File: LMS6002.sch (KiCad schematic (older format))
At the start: 52 parts, among them J1 SMA_H, J2 SMA_H, T1 B0322J5050, T2 B0322J5050, T3 TR_TC1-1-43X+, T4 TR_TC1-1-43X+, U12 BGS12, U13 BGS12, U3 LMS6002DR2

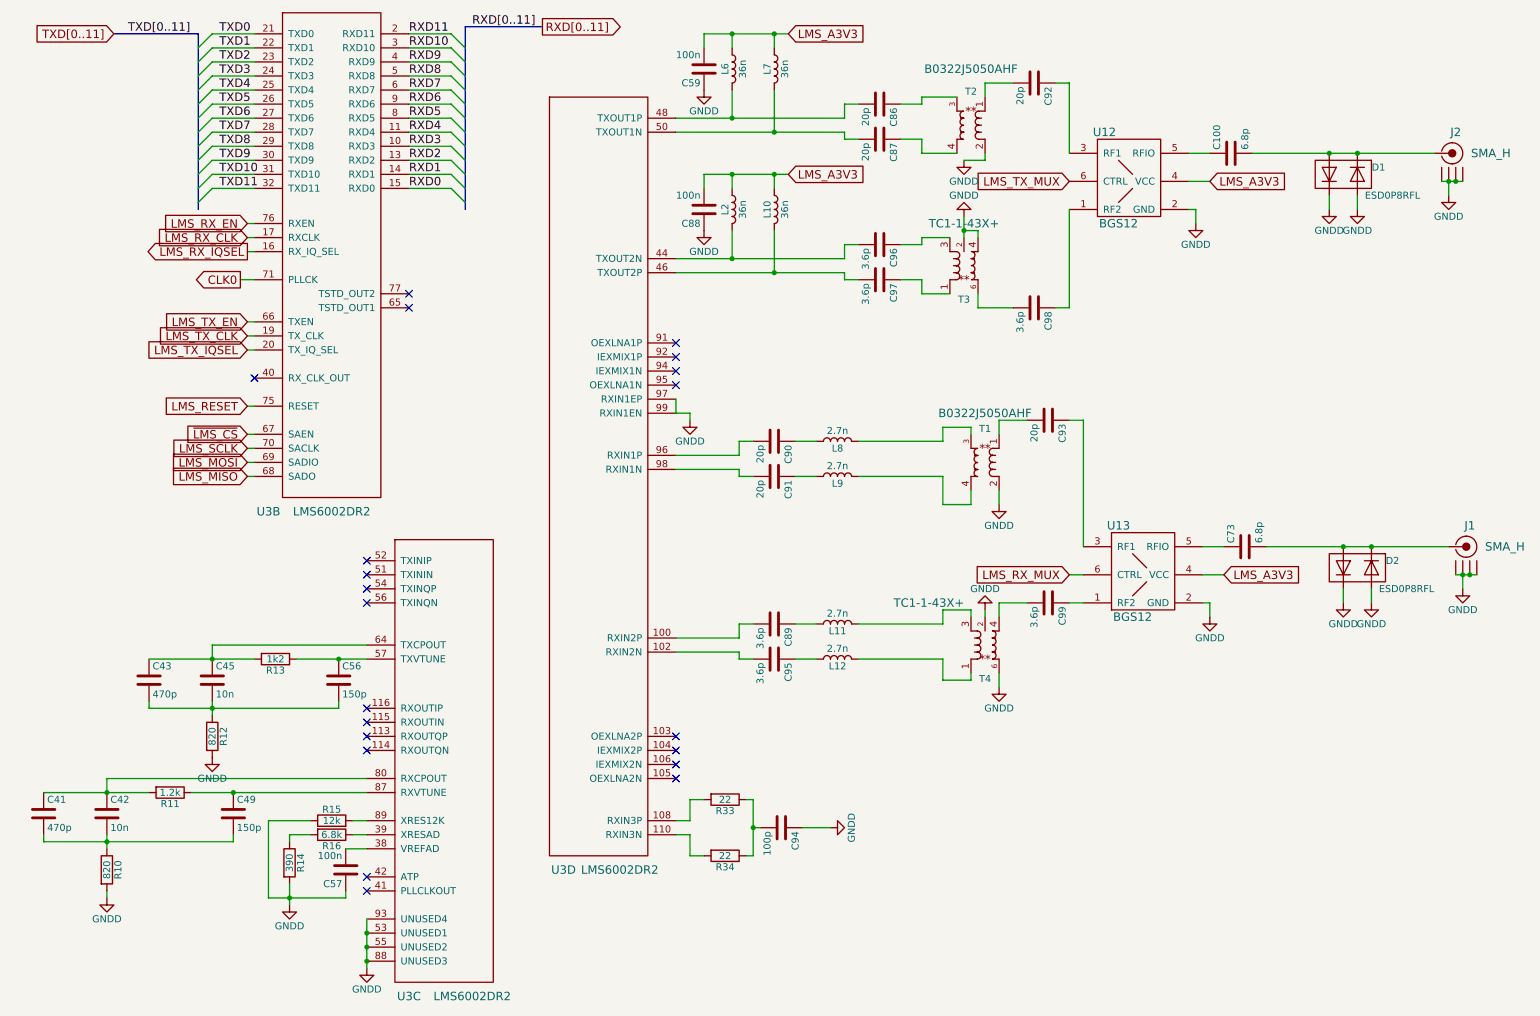
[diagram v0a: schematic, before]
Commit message: Preliminary placing top layer of RF
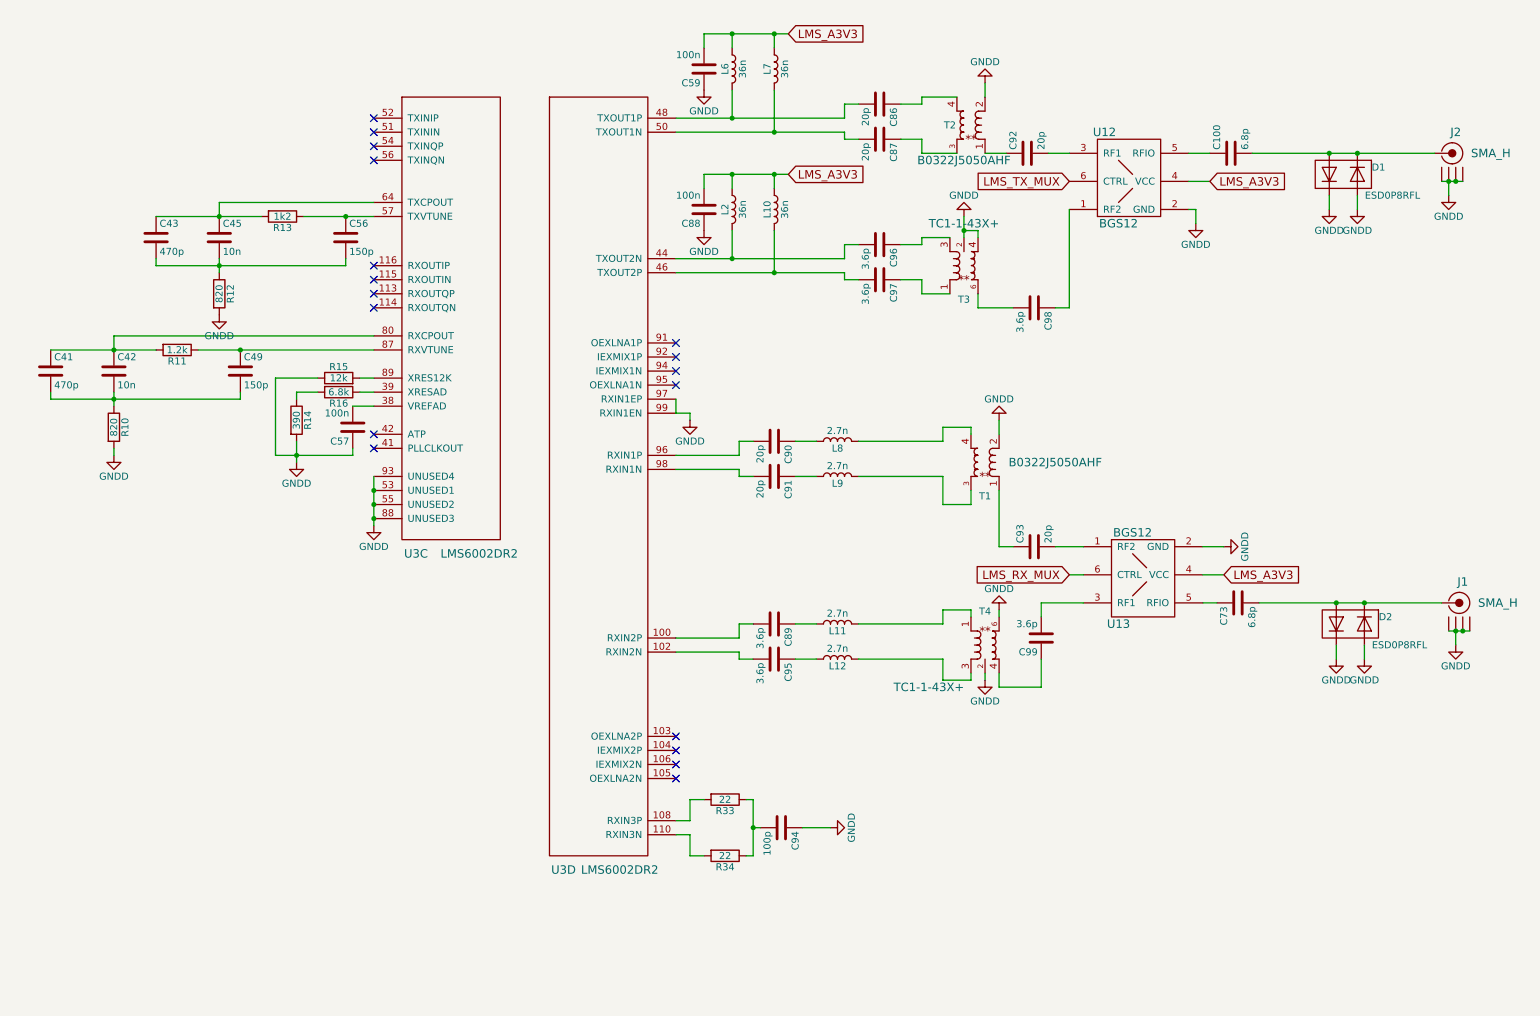
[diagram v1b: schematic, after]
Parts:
- removed unit 2 of U3
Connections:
- net at C87.1: now also T2.3; no longer T2.4
- net at C86.1: now also T2.4; no longer T2.3
- net at L8.2: now also T1.4; no longer T1.3
- net at L9.2: now also T1.3; no longer T1.4
- net at T2.1: now also C92.1; no longer C92.2
- net at T1.1: now also C93.1; no longer C93.2
- net at U12.3 (RF1): now also C92.2; no longer C92.1
- net at U13.3 (RF1): now also C99.2; no longer C93.1
- net at U13.1 (RF2): now also C93.2; no longer C99.1
- net at L11.2: now also T4.1; no longer T4.3
- net at L12.2: now also T4.3; no longer T4.1
- net at T4.4: now also C99.1; no longer C99.2
- no-connect marks 21 -> 18
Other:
- moved on the sheet: C41, C42, C43, C45, C49, C56, C57, C73, C92, C93, C99, D2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

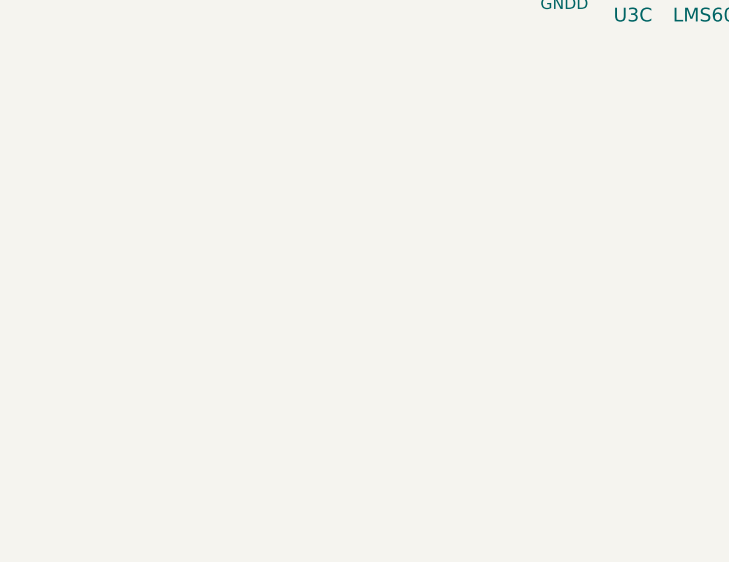
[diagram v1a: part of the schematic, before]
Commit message: Placement of RF is on going.
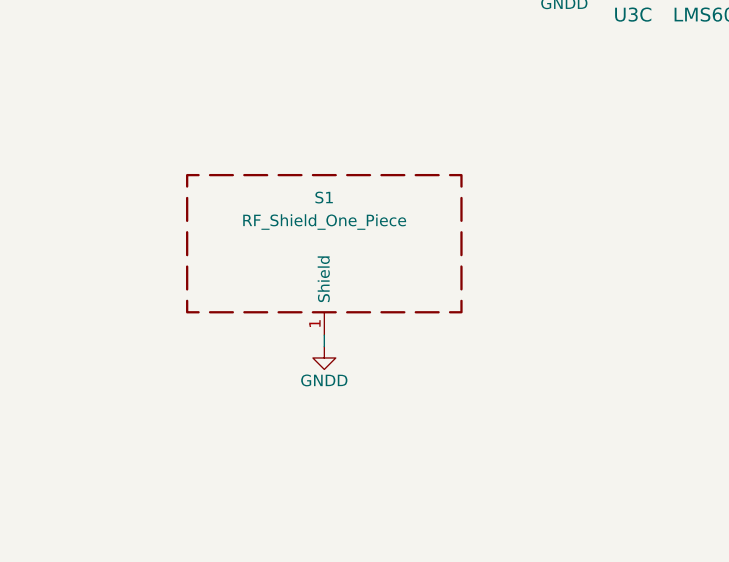
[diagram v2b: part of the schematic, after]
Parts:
- added S1: RF_Shield_One_Piece, sdr-foots:SHIELD, symbol RF_Shield_One_Piece
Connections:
- net GNDD: now also S1.1 (Shield)
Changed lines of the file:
@@
 Wire Wire Line
 	9050 4800 8950 4800
+$Comp
+L RF_Shield_One_Piece S1
+U 1 1 592DB799
+P 2000 5450
+F 0 "S1" H 2000 5650 50  0000 C CNN
+F 1 "RF_Shield_One_Piece" H 2000 5550 50  0000 C CNN
+F 2 "sdr-foots:SHIELD" H 2000 5350 50  0001 C CNN
+F 3 "" H 2000 5350 50  0001 C CNN
+	1    2000 5450
+	1    0    0    -1
+$EndComp
+$Comp
+L GNDD #PWR060
+U 1 1 592DBADE
+P 2000 5900
+F 0 "#PWR060" H 2000 5650 50  0001 C CNN
+F 1 "GNDD" H 2000 5750 50  0000 C CNN
+F 2 "" H 2000 5900 50  0000 C CNN
+F 3 "" H 2000 5900 50  0000 C CNN
+	1    2000 5900
+	1    0    0    -1
+$EndComp
+Wire Wire Line
+	2000 5900 2000 5850
 $EndSCHEMATC

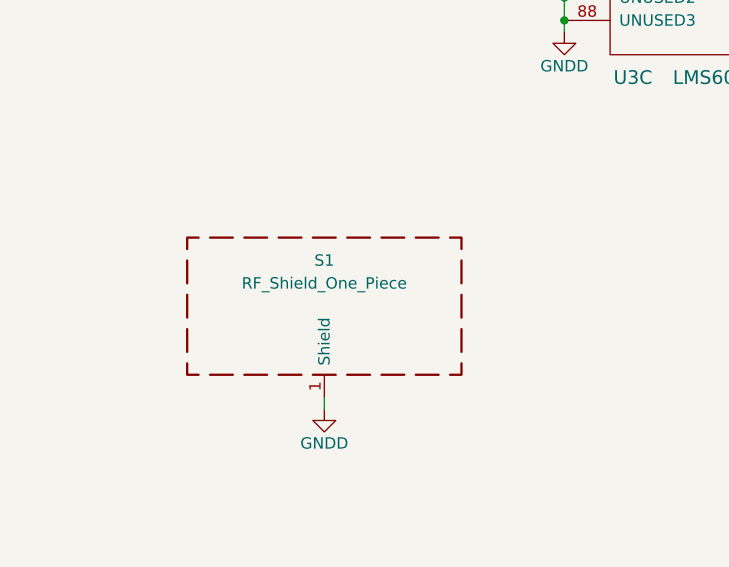
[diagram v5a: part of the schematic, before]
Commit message: Add schematic of FT232H. Not placed yet.
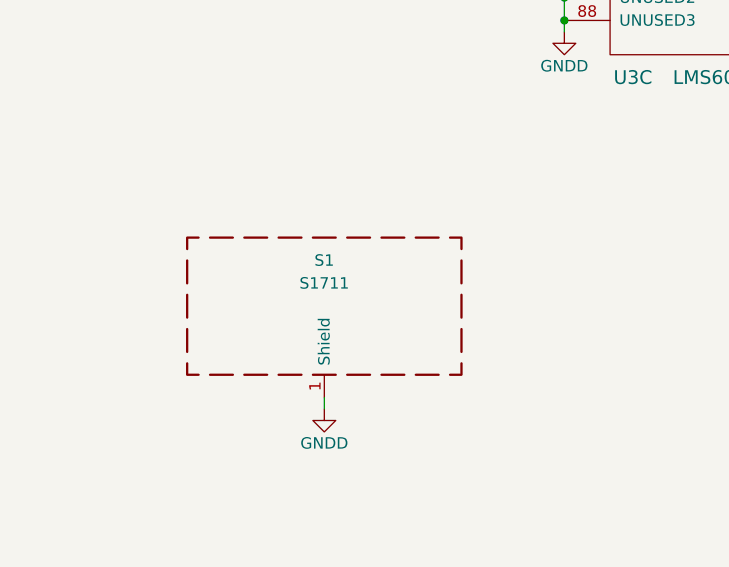
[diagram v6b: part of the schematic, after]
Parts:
- S1: value RF_Shield_One_Piece -> S1711
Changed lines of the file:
@@
 P 2000 5450
 F 0 "S1" H 2000 5650 50  0000 C CNN
-F 1 "RF_Shield_One_Piece" H 2000 5550 50  0000 C CNN
+F 1 "S1711" H 2000 5550 50  0000 C CNN
 F 2 "sdr-foots:SHIELD" H 2000 5350 50  0001 C CNN
 F 3 "" H 2000 5350 50  0001 C CNN

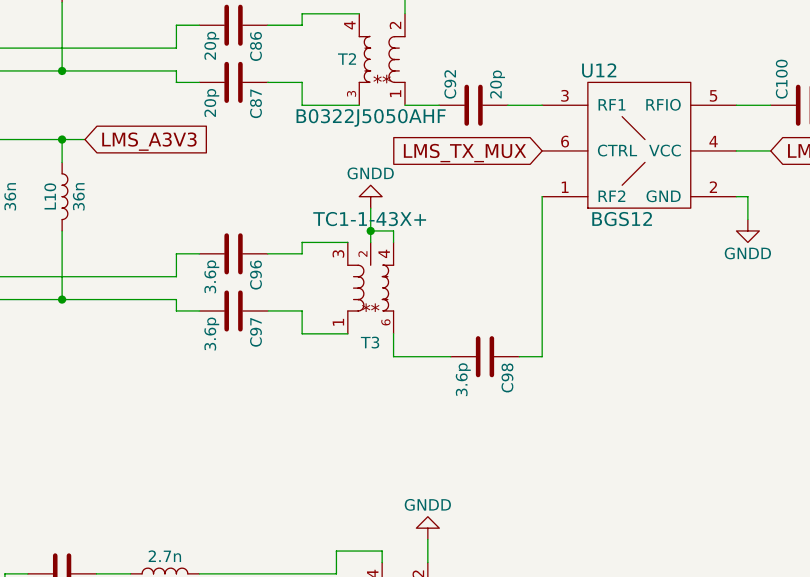
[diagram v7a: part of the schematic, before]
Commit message: Finish tracing. No DRC errors or unconnected nets. Put 2.5V reg on the top layer. Need to place RefDes on RF parts.
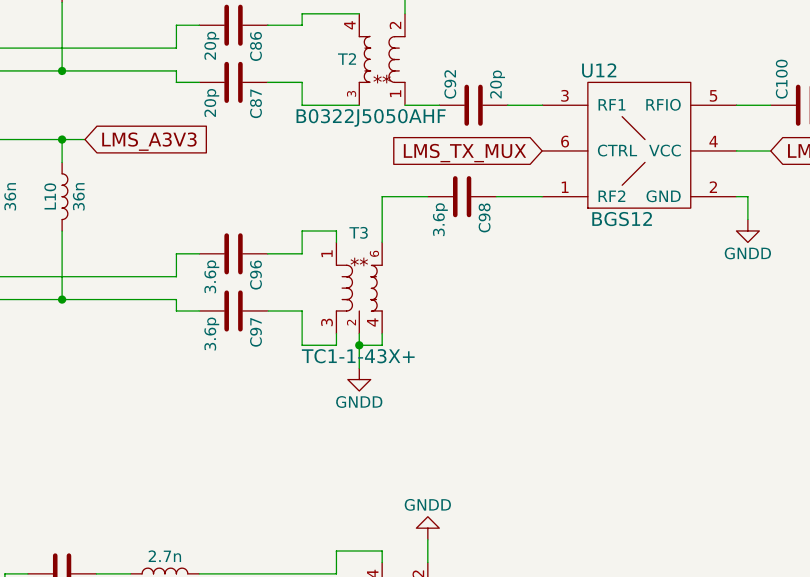
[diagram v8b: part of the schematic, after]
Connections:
- net at C97.1: now also T3.3; no longer T3.1
- net at C96.1: now also T3.1; no longer T3.3
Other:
- moved on the sheet: C98, T3
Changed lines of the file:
@@
 L TR_TC1-1-43X+ T3
 U 1 1 5923BD01
-P 7250 2400
-F 0 "T3" H 7250 2640 50  0000 C CNN
-F 1 "TR_TC1-1-43X+" H 7250 2775 50  0001 C CNN
-F 2 "sdr-foots:TC1-1-43X+" H 7275 2875 60  0001 C CNN
-F 3 "" H 7250 2640 60  0000 C CNN
-F 4 "Mini-Circuits" H 7300 3225 60  0001 C CNN "Manufacturer"
-F 5 "RF_Transformer;_650_-_4000_MHz;_RF_Power_0.25_Watt;_Ratio_1:1;_50_Ohm;" H 7475 3000 60  0001 C CNN "Description"
-F 6 "TC1-1-43X+" H 7375 3125 60  0001 C CNN "Manufacturer Part Number"
-F 7 "TC1-1-43X+" H 7300 3450 60  0001 C CNN "Vendor Part Number"
-F 8 "TC1-1-43X+" H 7250 2100 60  0000 C CNN "Component Value"
-	1    7250 2400
-	-1   0    0    1
+P 7200 2400
+F 0 "T3" H 7200 2640 50  0000 C CNN
+F 1 "TR_TC1-1-43X+" H 7200 2775 50  0001 C CNN
+F 2 "sdr-foots:TC1-1-43X+" H 7225 2875 60  0001 C CNN
+F 3 "" H 7200 2640 60  0000 C CNN
+F 4 "Mini-Circuits" H 7250 3225 60  0001 C CNN "Manufacturer"
+F 5 "RF_Transformer;_650_-_4000_MHz;_RF_Power_0.25_Watt;_Ratio_1:1;_50_Ohm;" H 7425 3000 60  0001 C CNN "Description"
+F 6 "TC1-1-43X+" H 7325 3125 60  0001 C CNN "Manufacturer Part Number"
+F 7 "TC1-1-43X+" H 7250 3450 60  0001 C CNN "Vendor Part Number"
+F 8 "TC1-1-43X+" H 7200 2100 60  0000 C CNN "Component Value"
+	1    7200 2400
+	-1   0    0    -1
 $EndComp
 $Comp
 L GNDD #PWR055
 U 1 1 5923C1B8
-P 7250 2050
-F 0 "#PWR055" H 7250 1800 50  0001 C CNN
-F 1 "GNDD" H 7250 1900 50  0000 C CNN
-F 2 "" H 7250 2050 50  0001 C CNN
-F 3 "" H 7250 2050 50  0001 C CNN
-	1    7250 2050
-	-1   0    0    1
+P 7200 2750
+F 0 "#PWR055" H 7200 2500 50  0001 C CNN
+F 1 "GNDD" H 7200 2600 50  0000 C CNN
+F 2 "" H 7200 2750 50  0001 C CNN
+F 3 "" H 7200 2750 50  0001 C CNN
+	1    7200 2750
+	-1   0    0    -1
 $EndComp
 $Comp
 L C C98
 U 1 1 5923C657
-P 7750 2700
-F 0 "C98" H 7775 2800 50  0000 L CNN
-F 1 "3.6p" H 7775 2600 50  0000 L CNN
-F 2 "Capacitors_SMD:C_0603" H 7788 2550 50  0001 C CNN
-F 3 "" H 7750 2700 50  0001 C CNN
-	1    7750 2700
+P 7650 2000
+F 0 "C98" H 7675 2100 50  0000 L CNN
+F 1 "3.6p" H 7675 1900 50  0000 L CNN
+F 2 "Capacitors_SMD:C_0603" H 7688 1850 50  0001 C CNN
+F 3 "" H 7650 2000 50  0001 C CNN
+	1    7650 2000
 	0    1    1    0
 $EndComp
@@
 Connection ~ 5900 2450
 Wire Wire Line
-	6800 2250 6950 2250
+	6950 2250 6800 2250
 Wire Wire Line
 	6950 2500 6800 2500
 Wire Wire Line
-	7250 2050 7250 2200
-Wire Wire Line
-	7150 2200 6950 2200
-Wire Wire Line
-	6950 2200 6950 2250
-Wire Wire Line
-	6950 2500 6950 2600
-Wire Wire Line
-	6950 2600 7150 2600
-Wire Wire Line
-	7350 2200 7350 2150
-Wire Wire Line
-	7350 2150 7250 2150
-Connection ~ 7250 2150
-Wire Wire Line
-	7600 2700 7350 2700
-Wire Wire Line
-	7350 2700 7350 2600
-Wire Wire Line
-	7900 2700 8000 2700
-Wire Wire Line
-	8000 2700 8000 2000
+	7200 2600 7200 2750
+Wire Wire Line
+	6950 2150 6950 2250
+Wire Wire Line
+	6950 2500 6950 2650
+Wire Wire Line
+	7300 2600 7300 2650
+Wire Wire Line
+	7300 2650 7200 2650
+Connection ~ 7200 2650
 Wire Wire Line
 	8900 2100 8900 2000
@@
 Wire Wire Line
 	2000 5900 2000 5850
+Wire Wire Line
+	6950 2150 7100 2150
+Wire Wire Line
+	7100 2150 7100 2200
+Wire Wire Line
+	7100 2600 7100 2650
+Wire Wire Line
+	7100 2650 6950 2650
+Wire Wire Line
+	8000 2000 7800 2000
+Wire Wire Line
+	7500 2000 7300 2000
+Wire Wire Line
+	7300 2000 7300 2200
 $EndSCHEMATC
